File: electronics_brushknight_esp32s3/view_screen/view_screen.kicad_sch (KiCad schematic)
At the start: 13 parts, among them J1 Conn_01x04, J2 GC9A01, J3 Conn_01x04, J4 Conn_01x04, J5 Conn_01x04, J6 LCD - FPC, Q1 2N7002

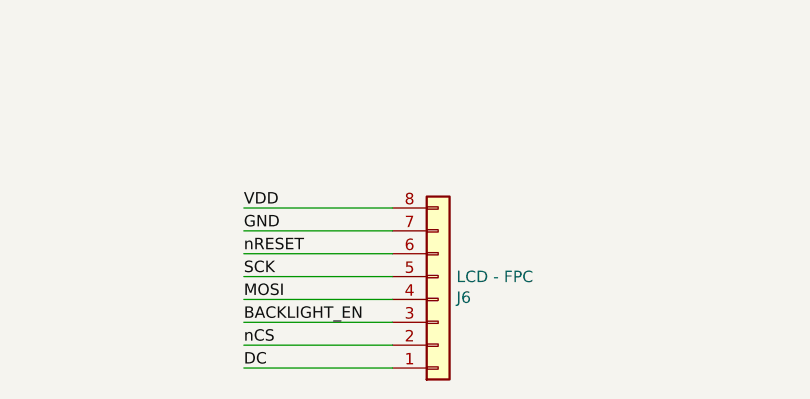
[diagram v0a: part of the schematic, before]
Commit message: Revert "DevKit PCB"
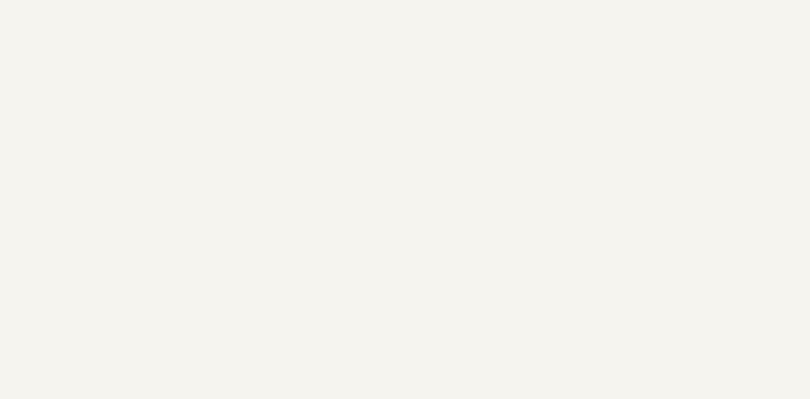
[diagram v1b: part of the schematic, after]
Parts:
- removed J6: LCD - FPC, screen_connector:Amphenol FCI FPC 8 pin 0.5 pitch, symbol Connector_Generic:Conn_01x08

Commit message: devkit pcb preview
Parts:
- added J6: LCD - FPC, screen_connector:Amphenol FCI FPC 8 pin 0.5 pitch, symbol Connector_Generic:Conn_01x08
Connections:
- net BACKLIGHT_EN: now also J6.3 (Pin_3)
- net DC: now also J6.1 (Pin_1)
- net GND: now also J6.7 (Pin_7)
- net MOSI: now also J6.4 (Pin_4)
- net SCK: now also J6.5 (Pin_5)
- net VDD: now also J6.8 (Pin_8)
- net nCS: now also J6.2 (Pin_2)
- net nRESET: now also J6.6 (Pin_6)
